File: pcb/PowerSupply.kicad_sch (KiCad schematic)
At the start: 1 part, among them U1 XL6019E1

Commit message: 1
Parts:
- removed U1: XL6019E1, lcsc_pro:TO-263-5_L10.2-W9.9-P1.70-LS14.4-TL, symbol lcsc_pro:XL6019E1
- added C1: 560p, symbol Device:C
- added C10, C11, C12, C13, C14: 10u, symbol Device:C
- added C15, C16: 180u, symbol Device:C
- added C17, C18, C19, C20, C21, C22: 4.7u, symbol Device:C
- added C2: 33n, symbol Device:C
- added C23, C24, C4, C5, C8: 0.1u, symbol Device:C
- added C25: 220p, symbol Device:C
- added C3, C9: 1u, symbol Device:C
- added C6: 1n, symbol Device:C
- added C7: 68u, symbol Device:C
- added D1: D, symbol Device:D
- added D2, D3: ~, Diode_THT:D_DO-41_SOD81_P10.16mm_Horizontal, symbol Diode:1N47xxA
- added L1: 4.7u, symbol Device:L
- added Q1, Q2, Q3, Q4: Q_NMOS_GDS, symbol Transistor_FET:Q_NMOS_GDS
- added R1, R4, R8: 10k, symbol Device:R
- added R10, R11, R13, R14: 100, symbol Device:R
- added R12: 8m, symbol Device:R
- added R15: 1.5k, symbol Device:R
- added R2: 27.4k, symbol Device:R
- added R3: 93.1k, symbol Device:R
- added R5: 59.0k, symbol Device:R
- added R6: 249k, symbol Device:R
- added R7: 2k, symbol Device:R
- added R9: 0, symbol Device:R
- added U1: LM5176PWP, Package_SO:HTSSOP-28-1EP_4.4x9.7mm_P0.65mm_EP3.4x9.5mm_ThermalVias, symbol Regulator_Switching:LM5176PWP
- added U2: RK097111080R, easyeda2kicad:RES-ADJ-TH_RK097111080R, symbol easyeda2kicad:RK097111080R
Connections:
- new net: Q3.3 (S), Q4.2 (D), R12.2, R13.1
- new net: C2.2, R1.1
- new net: C19.1, C20.2
- new net: C18.1, C19.2
- new net: C13.2, C14.1
- new net: C17.1, C18.2
- new net: C12.2, C13.1
- new net: C10.1, C11.1
- new net: C20.1, C21.2
- new net: D1.1 (K), R8.1
- new net: C15.1, C16.2
- new net: C11.2, C12.1
- new net Csync: C6.2
- new net GND: C1.2, C14.2, C16.1, C21.1, C25.2, C3.2, C4.2, C5.2, C7.2, C8.2, R1.2, R12.1, R14.1, R15.2, R2.2, R3.2, R5.2, U1.10 (AGND), U1.22 (PGND), U1.5 (DITH)
- new net Vin: C17.2, C7.1, D1.2 (A), Q1.2 (D), R6.1, R7.1
- new net Vout: C15.2, C9.1, R11.2, R9.1, U1.12 (VOSNS), U2.2
- new net bias: C4.1, U1.24 (BIAS)
- new net boot1: C23.1, D2.1 (K), U1.26 (BOOT1)
- new net boot2: C24.1, D3.1 (K), U1.20 (BOOT2)
- new net comp: C1.1, C2.1, U1.9 (COMP)
- new net cs: C22.1, R13.2, U1.16 (CS)
- new net csg: C22.2, R14.2, U1.15 (CSG)
- new net en/uvlo: R5.1, R6.2, U1.1 (EN/UVLO)
- new net fb: R15.1, U1.11 (FB), U2.3
- new net hdrv1: Q1.1 (G), U1.27 (HDRV1)
- new net hdrv2: Q2.1 (G), U1.19 (HDRV2)
- new net isns+: R10.1, U1.14 (ISNS(+))
- new net isns-: R11.1, U1.13 (ISNS(-))
- new net ldrv1: Q3.1 (G), U1.25 (LDRV1)
- new net ldrv2: Q4.1 (G), U1.21 (LDRV2)
- new net mode: R3.1, U1.4 (MODE)
- new net pgood: R4.1, U1.17 (PGOOD)
- new net powerPAD: U1.29 (PowerPAD)
- new net q2-2: C10.2, C9.2, Q2.2 (D), R10.2, R9.2
- new net q3-2: C23.2, L1.1, Q1.3 (S), Q3.2 (D), U1.28 (SW1)
- new net q4-2: C24.2, L1.2, Q2.3 (S), Q4.3 (S), U1.18 (SW2)
- new net rt/sync: C6.1, R2.1, U1.6 (RT/SYNC)
- new net slope: C25.1, U1.7 (SLOPE)
- new net ss: C5.1, U1.8 (SS)
- new net vcc: C3.1, D2.2 (A), D3.2 (A), R4.2, U1.23 (VCC)
- new net vin: C8.1, R8.2, U1.2 (VIN)
- new net visns: R7.2, U1.3 (VISNS)

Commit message: 添加子图 添加设计参数 修改en/uvlo 修改ss 更新10.0
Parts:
- added C26: 100n, symbol Device:C
- added J1: USB_C_Receptacle_PowerOnly_6P, symbol Connector:USB_C_Receptacle_PowerOnly_6P
- added R16: 470k, symbol Device:R
- added R17: 130k, symbol Device:R
- D2, D3: value ~ -> (none)
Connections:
- net GND: now also C26.1, R17.1; no longer U1.22 (PGND)
- net en/uvlo: no longer U1.1 (EN/UVLO)
- net ss: no longer U1.8 (SS)
- new net: J1.A12 (GND), J1.B12 (GND)
- new net: J1.A9 (VBUS), J1.B9 (VBUS)
- new net EN_UVLO: R16.1, R17.2, U1.1 (EN/UVLO)
- new net GNDPWR: U1.22 (PGND)
- new net SS: C26.2, U1.8 (SS)
- new net USB_VBUS: R16.2
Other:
- added sheet ch224k (ch224k.kicad_sch)
- note added: "延迟启动"
- note added: "开机电压设置 低压保护"
- moved on the sheet: U1

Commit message: vin
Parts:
- added C27: 100n 63V, symbol Device:C
- added R18: 10R, symbol Device:R
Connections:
- net GND: now also C27.1
- net USB_VBUS: now also R18.2
- net vin: no longer U1.2 (VIN)
- new net VIN: C27.2, R18.1, U1.2 (VIN)
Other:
- note added: "电源RC滤波"

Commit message: boot vcc
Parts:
- added C28: 1u, symbol Device:C
- added C29: 100n, symbol Device:C
- added D4: SS14, Diode_SMD:D_SMA, symbol Diode:SS14
- added D5: SS310, Diode_SMD:D_SMA, symbol Diode:SS310
- added R19: 2k, symbol Device:R
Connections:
- net GND: now also C28.1
- net USB_VBUS: now also D4.2 (A), R19.2; no longer R18.2
- net boot1: no longer U1.26 (BOOT1)
- net boot2: no longer U1.20 (BOOT2)
- net q3-2: no longer U1.28 (SW1)
- net vcc: no longer U1.23 (VCC)
- net visns: no longer U1.3 (VISNS)
- new net: D4.1 (K), R18.2
- new net BOOT1: C29.2, D5.1 (K), U1.26 (BOOT1)
- new net BOOT2: U1.20 (BOOT2)
- new net SW1: C29.1, U1.28 (SW1)
- new net VCC: C28.2, D5.2 (A), U1.23 (VCC)
- new net VISNS: R19.1, U1.3 (VISNS)
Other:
- note added: "VCC滤波"
- note added: "电源RC滤波 二极管需耐压20V，小于0.8V压降"
- note added: "输入电压检测脚"
- note removed: "电源RC滤波"

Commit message: first teach
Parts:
- removed J1: USB_C_Receptacle_PowerOnly_6P, symbol Connector:USB_C_Receptacle_PowerOnly_6P
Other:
- added sheet stm32 (stm32.kicad_sch)
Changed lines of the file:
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@@
 	)
 	(symbol
-		(lib_id "Connector:USB_C_Receptacle_PowerOnly_6P")
-		(at 781.05 71.12 0)
-		(unit 1)
-		(body_style 1)
-		(exclude_from_sim no)
-		(in_bom yes)
-		(on_board yes)
-		(in_pos_files yes)
-		(dnp no)
-		(fields_autoplaced yes)
-		(property "Reference" "J1"
-			(at 781.05 53.34 0)
-			(show_name no)
-			(do_not_autoplace no)
-			(effects
-				(font
-					(size 1.27 1.27)
-				)
-			)
-		)
-		(property "Value" "USB_C_Receptacle_PowerOnly_6P"
-			(at 781.05 55.88 0)
-			(show_name no)
-			(do_not_autoplace no)
-			(effects
-				(font
-					(size 1.27 1.27)
-				)
-			)
-		)
-		(property "Footprint" ""
-			(at 784.86 68.58 0)
-			(hide yes)
-			(show_name no)
-			(do_not_autoplace no)
-			(effects
-				(font
-					(size 1.27 1.27)
-				)
-			)
-		)
-		(property "Datasheet" "https://www.usb.org/sites/default/files/documents/usb_type-c.zip"
-			(at 781.05 71.12 0)
-			(hide yes)
-			(show_name no)
-			(do_not_autoplace no)
-			(effects
-				(font
-					(size 1.27 1.27)
-				)
-			)
-		)
-		(property "Description" "USB Power-Only 6P Type-C Receptacle connector"
-			(at 781.05 71.12 0)
-			(hide yes)
-			(show_name no)
-			(do_not_autoplace no)
-			(effects
-				(font
-					(size 1.27 1.27)
-				)
-			)
-		)
-		(pin "A9"
-		)
-		(pin "B9"
-		)
-		(pin "A5"
-		)
-		(pin "B5"
-		)
-		(pin "SH"
-		)
-		(pin "B12"
-		)
-		(pin "A12"
-		)
-		(instances
-			(project "PowerSupply"
-				(path "/3ecbe32c-4290-401a-9b8c-a7a0b4ba8879"
-					(reference "J1")
-					(unit 1)
-				)
-			)
-		)
-	)
-	(symbol
 		(lib_id "Device:C")
 		(at 64.77 158.75 270)
@@
 				)
 			)
+		)
+	)
+	(sheet
+		(at 640.08 -306.07)
+		(size 513.08 290.83)
+		(exclude_from_sim no)
+		(in_bom yes)
+		(on_board yes)
+		(dnp no)
+		(fields_autoplaced yes)
+		(stroke
+			(width 0.1524)
+			(type solid)
+		)
+		(fill
+			(color 0 0 0 0)
+		)
+		(property "Sheetname" "stm32"
+			(at 640.08 -306.7816 0)
+			(show_name no)
+			(do_not_autoplace no)
+			(effects
+				(font
+					(size 1.27 1.27)
+				)
+				(justify left bottom)
+			)
+		)
+		(property "Sheetfile" "stm32.kicad_sch"
+			(at 640.08 -14.6554 0)
+			(show_name no)
+			(do_not_autoplace no)
+			(effects
+				(font
+					(size 1.27 1.27)
+				)
+				(justify left top)
+			)
+		)
+		(instances
+			(project "PowerSupply"
+				(path "/3ecbe32c-4290-401a-9b8c-a7a0b4ba8879"
+					(page "3")
+				)
+			)

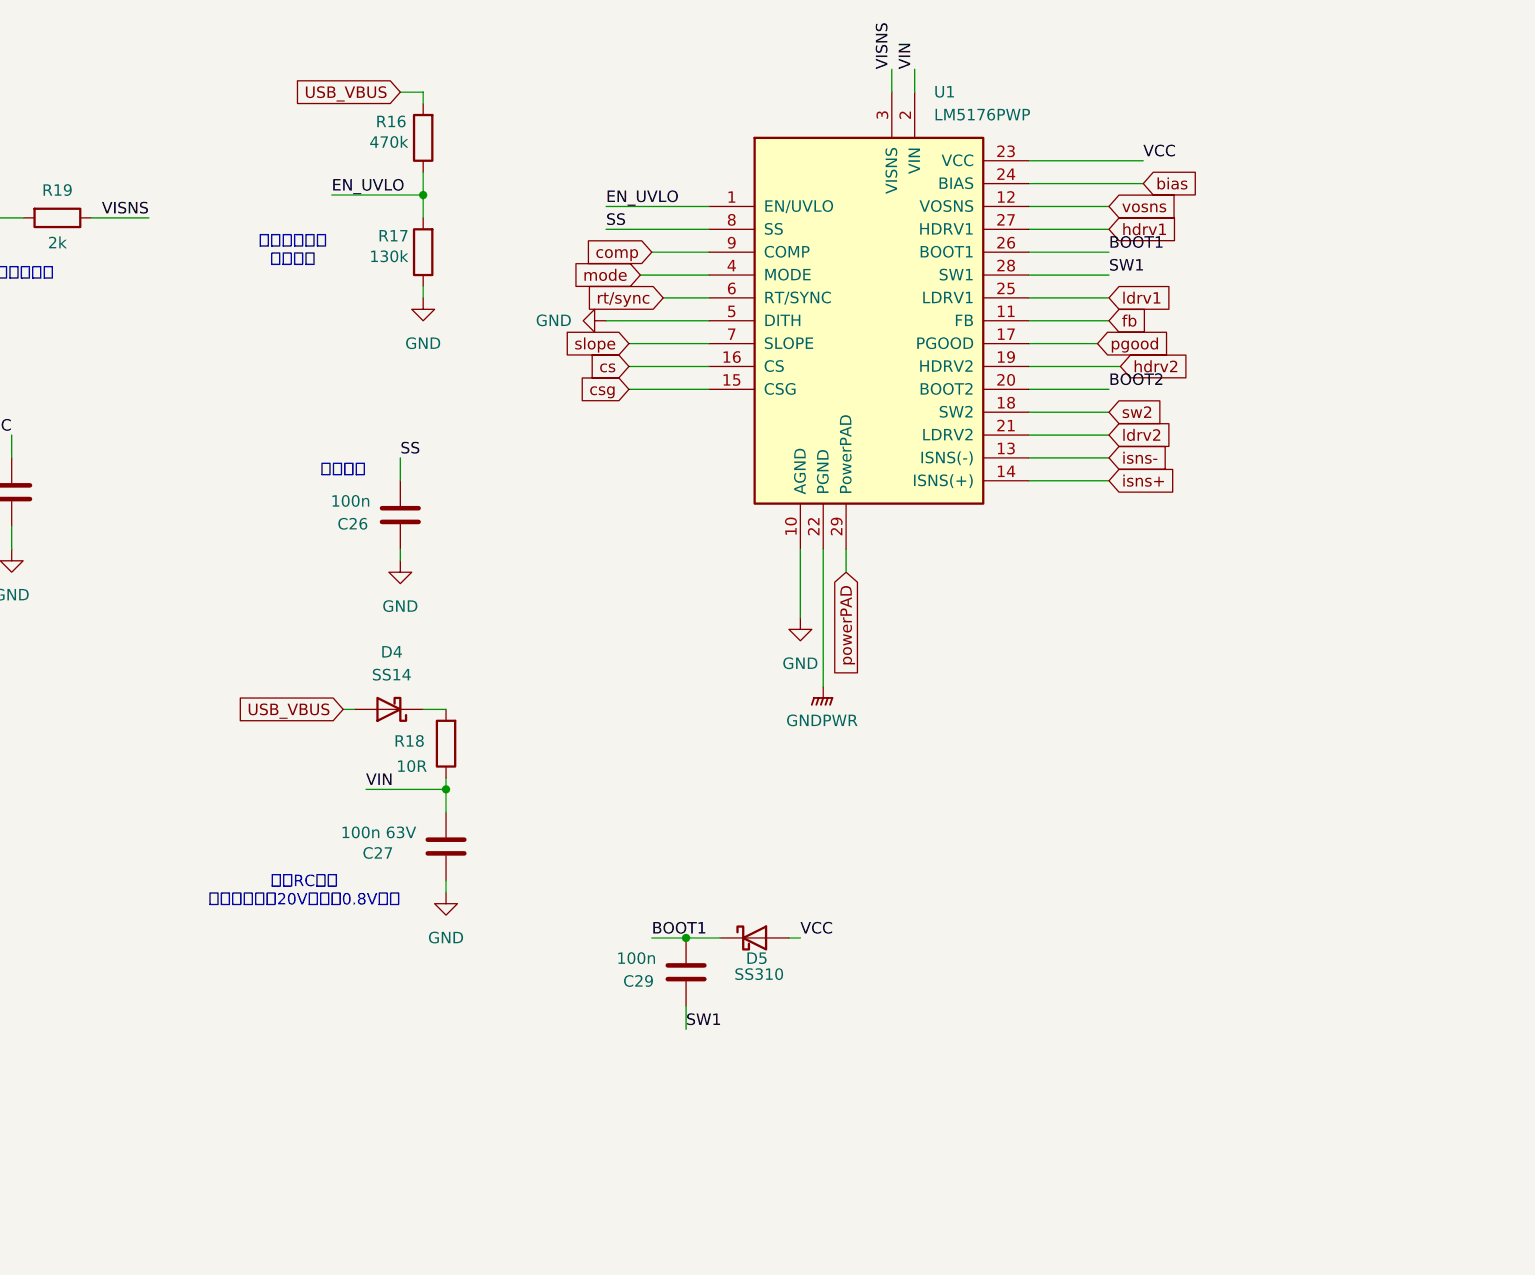
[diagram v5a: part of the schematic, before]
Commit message: BIAS电路 MOS选择
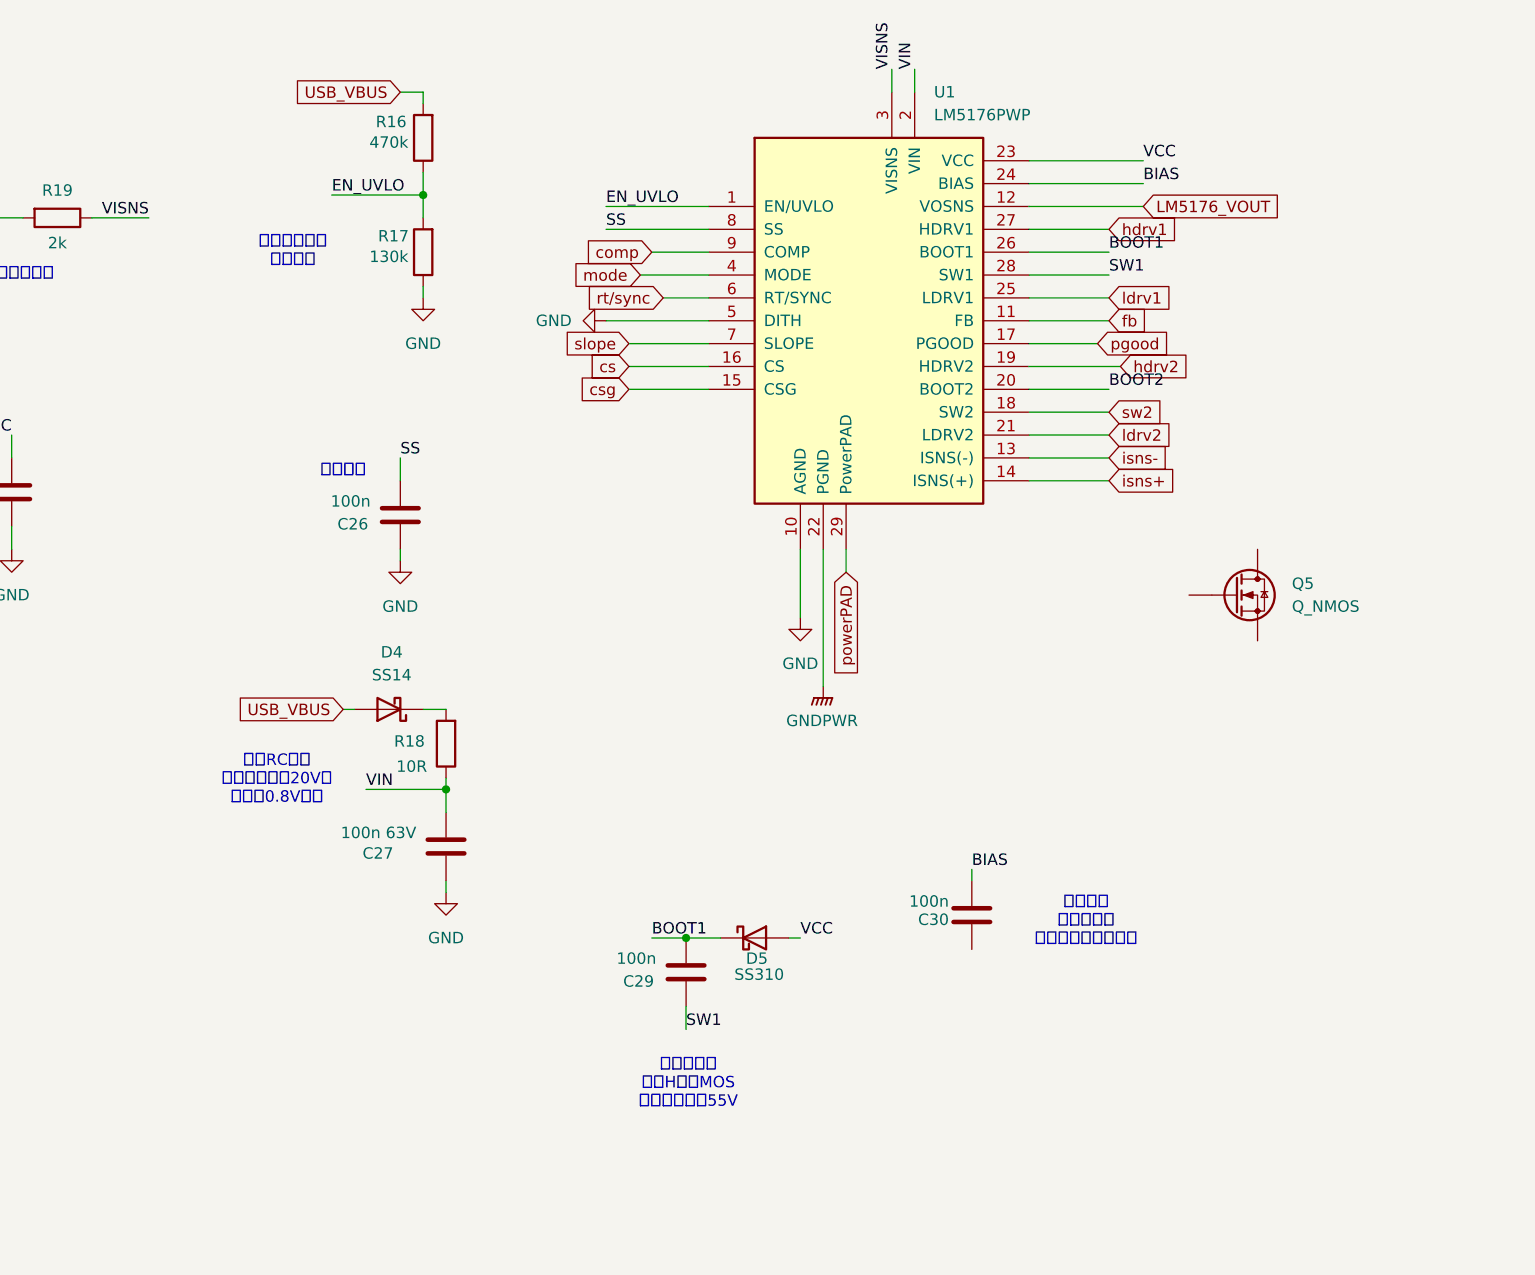
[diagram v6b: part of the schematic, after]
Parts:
- added C30: 100n, symbol Device:C
- added Q5: Q_NMOS, symbol Device:Q_NMOS
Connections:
- net Vout: no longer U1.12 (VOSNS)
- net bias: no longer U1.24 (BIAS)
- new net BIAS: C30.2, U1.24 (BIAS)
- new net LM5176_VOUT: U1.12 (VOSNS)
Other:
- note added: "低压供电 暂时不连， 因为找不到合适电源"
- note added: "电源RC滤波 二极管需耐压20V， 且小于0.8V压降"
- note added: "自举电容， 驱动H部分MOS 二极管需耐压55V"
- note removed: "电源RC滤波 二极管需耐压20V，小于0.8V压降"
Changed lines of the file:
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@@
 	(generator_version "10.0")
 	(paper "A2")
-	(text "电源RC滤波\n二极管需耐压20V，小于0.8V压降"
+	(text "电源RC滤波\n二极管需耐压20V，\n且小于0.8V压降"
 		(exclude_from_sim no)
-		(at 226.822 218.44 0)
+		(at 223.774 205.994 0)
 		(effects
 			(font
@@
 		)
 	)
+	(text "低压供电\n暂时不连，\n因为找不到合适电源"
+		(exclude_from_sim no)
+		(at 313.69 221.742 0)
+		(effects
+			(font
+				(size 1.27 1.27)
+			)
+		)
+	)
 	(text "VCC滤波"
 		(exclude_from_sim no)
@@
 		)
 	)
+	(text "自举电容，\n驱动H部分MOS\n二极管需耐压55V"
+		(exclude_from_sim no)
+		(at 269.494 239.776 0)
+		(effects
+			(font
+				(size 1.27 1.27)
+			)
+		)
+	)
 	(junction
 		(at 38.1 158.75)
@@
 	(wire
 		(pts
+			(xy 300.99 215.9) (xy 300.99 217.17)
+		)
+		(stroke
+			(width 0)
+			(type default)
+		)
+	)
+	(wire
+		(pts
 			(xy 44.45 214.63) (xy 44.45 215.9)
 		)
@@
 	(wire
 		(pts
-			(xy 307.34 142.24) (xy 316.23 142.24)
+			(xy 307.34 142.24) (xy 320.04 142.24)
 		)
 		(stroke
@@
 		)
 	)
+	(label "BIAS"
+		(at 300.99 215.9 0)
+		(effects
+			(font
+				(size 1.27 1.27)
+			)
+			(justify left bottom)
+		)
+	)
 	(label "BOOT2"
 		(at 316.23 162.56 0)
@@
 		)
 	)
+	(label "BIAS"
+		(at 320.04 139.7 0)
+		(effects
+			(font
+				(size 1.27 1.27)
+			)
+			(justify left bottom)
+		)
+	)
 	(label "SW1"
 		(at 269.24 233.68 0)
@@
 		)
 	)
+	(global_label "LM5176_VOUT"
+		(shape input)
+		(at 320.04 142.24 0)
+		(fields_autoplaced yes)
+		(effects
+			(font
+				(size 1.27 1.27)
+			)
+			(justify left)
+		)
+		(property "Intersheetrefs" "${INTERSHEET_REFS}"
+			(at 336.0275 142.24 0)
+			(hide yes)
+			(show_name no)
+			(do_not_autoplace no)
+			(effects
+				(font
+					(size 1.27 1.27)
+				)
+				(justify left)
+			)
+		)
+	)
 	(global_label "slope"
 		(shape input)
@@
 		)
 	)
-	(global_label "bias"
-		(shape input)
-		(at 320.04 139.7 0)
-		(fields_autoplaced yes)
-		(effects
-			(font
-				(size 1.27 1.27)
-			)
-			(justify left)
-		)
-		(property "Intersheetrefs" "${INTERSHEET_REFS}"
-			(at 326.9561 139.7 0)
-			(hide yes)
-			(show_name no)
-			(do_not_autoplace no)
-			(effects
-				(font
-					(size 1.27 1.27)
-				)
-				(justify left)
-			)
-		)
-	)
 	(global_label "hdrv1"
 		(shape input)
@@
 		)
 	)
-	(global_label "vosns"
-		(shape input)
-		(at 316.23 142.24 0)
-		(fields_autoplaced yes)
-		(effects
-			(font
-				(size 1.27 1.27)
-			)
-			(justify left)
-		)
-		(property "Intersheetrefs" "${INTERSHEET_REFS}"
-			(at 324.537 142.24 0)
-			(hide yes)
-			(show_name no)
-			(do_not_autoplace no)
-			(effects
-				(font
-					(size 1.27 1.27)
-				)
-				(justify left)
-			)
-		)
-	)
 	(global_label "sw2"
 		(shape input)
@@
 	)
 	(symbol
+		(lib_id "Device:Q_NMOS")
+		(at 330.2 185.42 0)
+		(unit 1)
+		(body_style 1)
+		(exclude_from_sim no)
+		(in_bom yes)
+		(on_board yes)
+		(in_pos_files yes)
+		(dnp no)
+		(fields_autoplaced yes)
+		(property "Reference" "Q5"
+			(at 336.55 184.1499 0)
+			(show_name no)
+			(do_not_autoplace no)
+			(effects
+				(font
+					(size 1.27 1.27)
+				)
+				(justify left)
+			)
+		)
+		(property "Value" "Q_NMOS"
+			(at 336.55 186.6899 0)
+			(show_name no)
+			(do_not_autoplace no)
+			(effects
+				(font
+					(size 1.27 1.27)
+				)
+				(justify left)
+			)
+		)
+		(property "Footprint" ""
+			(at 335.28 182.88 0)
+			(hide yes)
+			(show_name no)
+			(do_not_autoplace no)
+			(effects
+				(font
+					(size 1.27 1.27)
+				)
+			)
+		)
+		(property "Datasheet" ""
+			(at 330.2 185.42 0)
+			(hide yes)
+			(show_name no)
+			(do_not_autoplace no)
+			(effects
+				(font
+					(size 1.27 1.27)
+				)
+			)
+		)
+		(property "Description" "N-MOSFET transistor"
+			(at 330.2 185.42 0)
+			(hide yes)
+			(show_name no)
+			(do_not_autoplace no)
+			(effects
+				(font
+					(size 1.27 1.27)
+				)
+			)
+		)
+		(pin "G"
+		)
+		(pin "D"
+		)
+		(pin "S"
+		)
+		(instances
+			(project "PowerSupply"
+				(path "/3ecbe32c-4290-401a-9b8c-a7a0b4ba8879"
+					(reference "Q5")
+					(unit 1)
+				)
+			)
+		)
+	)
+	(symbol
 		(lib_id "Device:C")
 		(at 146.05 36.83 0)
@@
 					(unit 1)
 				)
+			)
+		)
+	)
+	(symbol
+		(lib_id "Device:C")
+		(at 300.99 220.98 180)
+		(unit 1)
+		(body_style 1)
+		(exclude_from_sim no)
+		(in_bom yes)
+		(on_board yes)
+		(in_pos_files yes)
+		(dnp no)
+		(property "Reference" "C30"
+			(at 298.45 221.488 0)
+			(show_name no)
+			(do_not_autoplace no)
+			(effects
+				(font
+					(size 1.27 1.27)
+				)
+				(justify left)
+			)
+		)
+		(property "Value" "100n"
+			(at 298.45 219.456 0)
+			(show_name no)
+			(do_not_autoplace no)
+			(effects
+				(font
+					(size 1.27 1.27)
+				)
+				(justify left)
+			)
+		)
+		(property "Footprint" ""
+			(at 300.0248 217.17 0)
+			(hide yes)
+			(show_name no)
+			(do_not_autoplace no)
+			(effects
+				(font
+					(size 1.27 1.27)
+				)
+			)
+		)
+		(property "Datasheet" ""
+			(at 300.99 220.98 0)
+			(hide yes)
+			(show_name no)
+			(do_not_autoplace no)
+			(effects
+				(font
+					(size 1.27 1.27)
+				)
+			)
+		)
+		(property "Description" "Unpolarized capacitor"
+			(at 300.99 220.98 0)
+			(hide yes)
+			(show_name no)
+			(do_not_autoplace no)
+			(effects
+				(font
+					(size 1.27 1.27)
+				)
+			)
+		)
+		(pin "2"
+		)
+		(pin "1"
+		)
+		(instances
+			(project "PowerSupply"
+				(path "/3ecbe32c-4290-401a-9b8c-a7a0b4ba8879"
+					(reference "C30")
+					(unit 1)
+				)

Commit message: mos电路
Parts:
- added C31: 47p, symbol Device:C
- added L2: 4.7u, symbol Device:L
- added Q6, Q7, Q8: Q_NMOS, symbol Device:Q_NMOS
- added R21: 93.1k, symbol Device:R
- added R22: 8m, symbol Device:R
- added R23, R24: 10R, symbol Device:R
- Q1: footprint (none) -> Package_DFN_QFN:DFN-8-1EP_6x5mm_P1.27mm_EP2x2mm
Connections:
- net GND: now also C30.1, R21.1
- net GNDPWR: now also R22.1, R24.1
- net USB_VBUS: now also Q5.D
- net cs: no longer U1.16 (CS)
- net csg: no longer U1.15 (CSG)
- net hdrv1: no longer U1.27 (HDRV1)
- net hdrv2: no longer U1.19 (HDRV2)
- net ldrv1: no longer U1.25 (LDRV1)
- net ldrv2: no longer U1.21 (LDRV2)
- net mode: no longer U1.4 (MODE)
- net HDRV1: now reaches Q5.G
- net HDRV1: now also U1.27 (HDRV1)
- net at Q5.S: now also L2.1, Q8.D
- new net: L2.2, Q6.S, Q7.D
- new net: Q7.S, Q8.S, R22.2, R23.1
- new net CS: C31.2, R23.2, U1.16 (CS)
- new net CSG: C31.1, R24.2, U1.15 (CSG)
- new net HDRV2: Q6.G, U1.19 (HDRV2)
- new net LDRV1: Q8.G, U1.25 (LDRV1)
- new net LDRV2: Q7.G, U1.21 (LDRV2)
- new net MODE: R21.2, U1.4 (MODE)
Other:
- note added: "开关电路 MOS需N，且耐压55V 大电感减小最大电压差，减小纹波 小电感增加响应速度"
- note added: "模式选择 开启hiccup和CCM"
- note added: "电感电流采样电路 的滤波"
- moved on the sheet: Q5
